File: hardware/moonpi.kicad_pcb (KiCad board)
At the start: 4 copper layers, 60 x 60 mm, 121 parts, among them J1 JAE_SIM_Card_SF72S006, J11 Micro_SD_Card, J2 UART, J3 Bus_PCI_Express_Mini, J4 USB_C_Receptacle, J8 HR911105_RJ45, SW2 SW_MEC_5G, U1 AllwinnerV3S, U10 TLV62568DBV, U2 CH340C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

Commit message: Changed USB series termination resistors values to zero-ohm
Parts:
- R24, R25: value 33R -> 0R

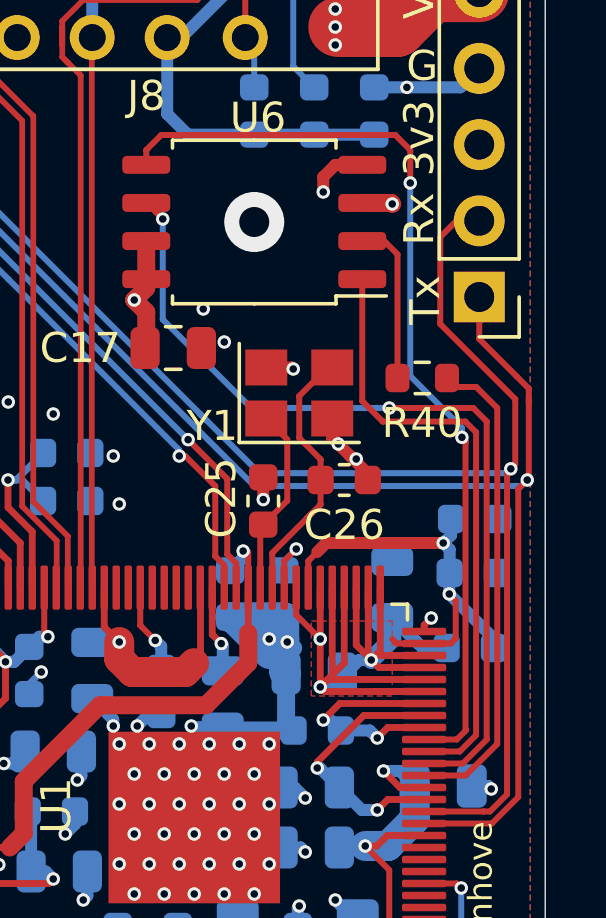
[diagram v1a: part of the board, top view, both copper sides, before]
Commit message: FIX: Added pull-up on SPI /CS
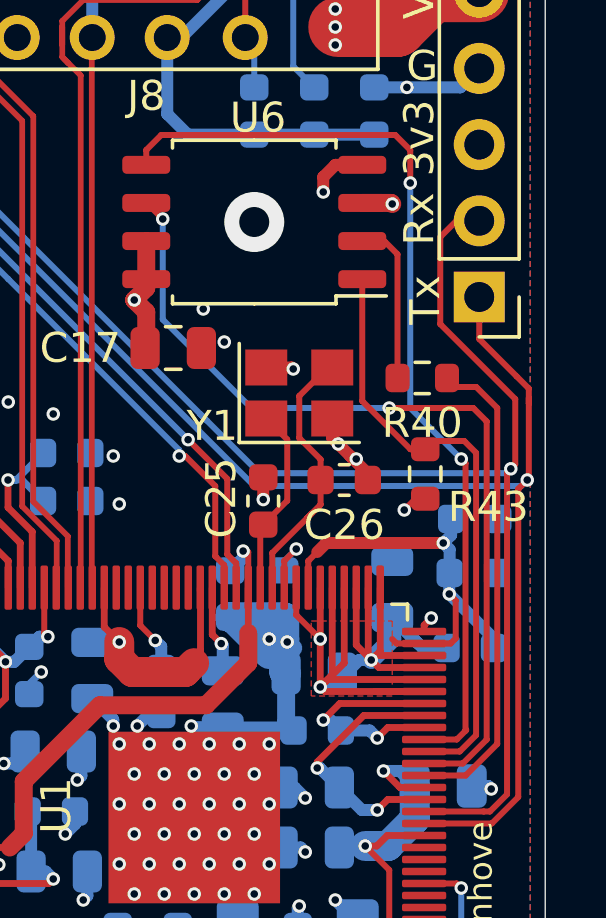
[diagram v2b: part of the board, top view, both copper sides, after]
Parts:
- added R43: 10k, Resistor_SMD:R_0603_1608Metric, F.Cu at (118.0, 105.0)
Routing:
- net +3V3: track 174.7 -> 175.6 mm, vias 34 -> 35
